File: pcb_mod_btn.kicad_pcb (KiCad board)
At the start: 2 copper layers, 116.1 x 100.1 mm, 50 parts, among them J1 leds_1, J10 leds_2, J11 led_3, J12 btn_3, J13 leds_4, J14 leds_4, J15 leds_4, J16 leds_4, J17 btn_4, J18 leds_5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

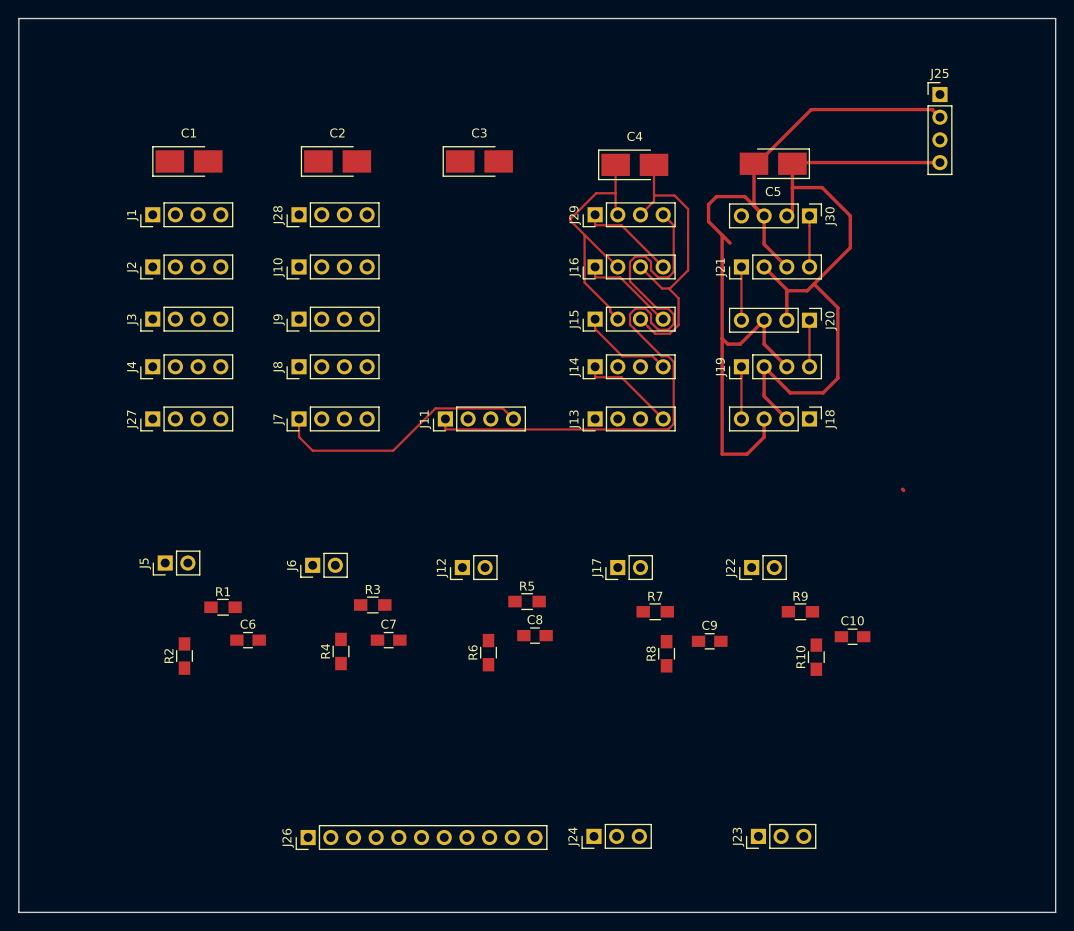
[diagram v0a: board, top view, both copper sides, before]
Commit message: footprints para tornillos, modulo botones terminado, todo marcas pin 1 headers
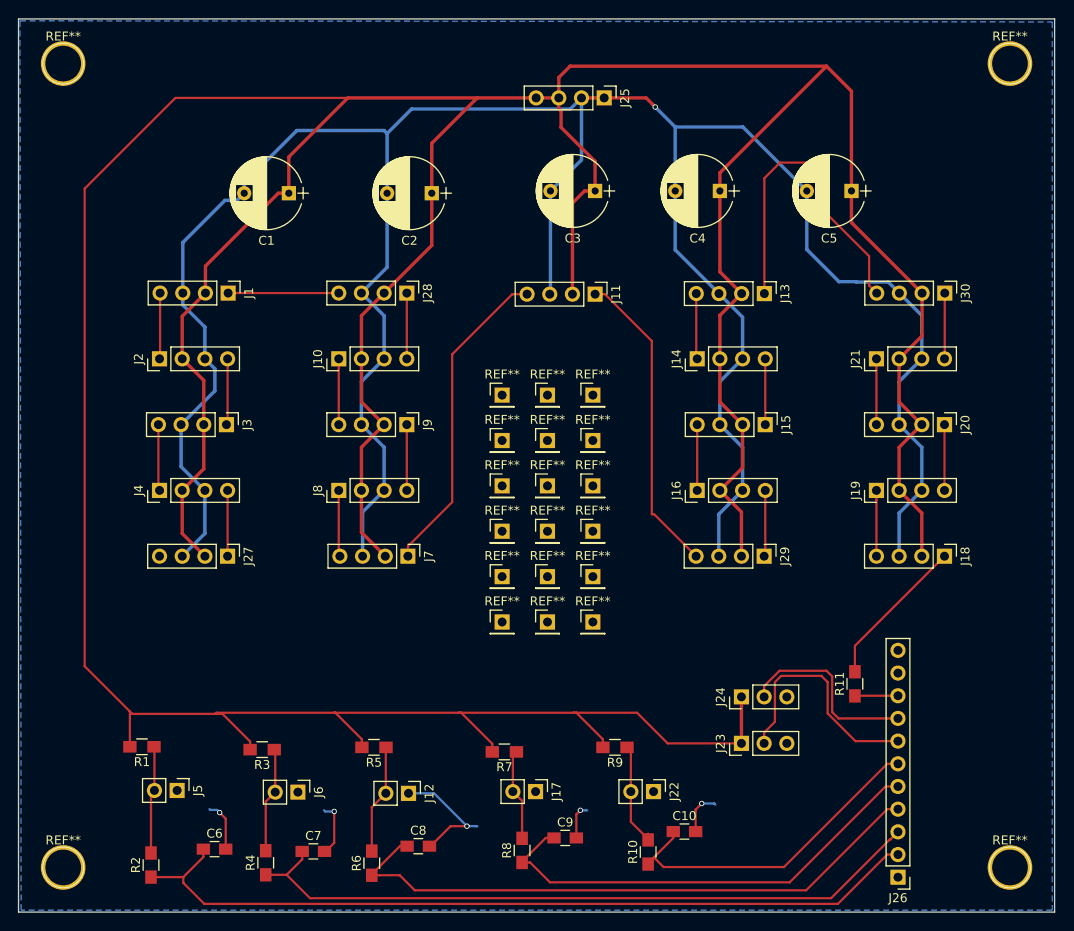
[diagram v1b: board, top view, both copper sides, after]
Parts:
- added R11: 240ohm, Resistors_SMD:R_0805_HandSoldering, F.Cu at (143.6, 103.4)
- added REF**: , Pin_Headers:Pin_Header_Straight_1x01_Pitch2.54mm, F.Cu at (114.3, 96.5)
- added REF**: , Pin_Headers:Pin_Header_Straight_1x01_Pitch2.54mm, F.Cu at (109.2, 86.4)
- added REF**: , Pin_Headers:Pin_Header_Straight_1x01_Pitch2.54mm, F.Cu at (104.1, 86.4)
- added REF**: , Pin_Headers:Pin_Header_Straight_1x01_Pitch2.54mm, F.Cu at (114.3, 86.4)
- added REF**: , Pin_Headers:Pin_Header_Straight_1x01_Pitch2.54mm, F.Cu at (114.3, 76.2)
- added REF**: , Pin_Headers:Pin_Header_Straight_1x01_Pitch2.54mm, F.Cu at (104.1, 76.2)
- added REF**: , Pin_Headers:Pin_Header_Straight_1x01_Pitch2.54mm, F.Cu at (109.2, 76.2)
- added REF**: 1pin, footprints:1pin, F.Cu at (161.0, 34.0)
- added REF**: 1pin, footprints:1pin, F.Cu at (55.0, 34.0)
- added REF**: 1pin, footprints:1pin, F.Cu at (55.0, 124.0)
- added REF**: 1pin, footprints:1pin, F.Cu at (161.0, 124.0)
- added REF**: , Pin_Headers:Pin_Header_Straight_1x01_Pitch2.54mm, F.Cu at (104.1, 96.5)
- added REF**: , Pin_Headers:Pin_Header_Straight_1x01_Pitch2.54mm, F.Cu at (109.2, 71.1)
- added REF**: , Pin_Headers:Pin_Header_Straight_1x01_Pitch2.54mm, F.Cu at (104.1, 71.1)
- added REF**: , Pin_Headers:Pin_Header_Straight_1x01_Pitch2.54mm, F.Cu at (114.3, 71.1)
- added REF**: , Pin_Headers:Pin_Header_Straight_1x01_Pitch2.54mm, F.Cu at (109.2, 96.5)
- added REF**: , Pin_Headers:Pin_Header_Straight_1x01_Pitch2.54mm, F.Cu at (109.2, 91.4)
- added REF**: , Pin_Headers:Pin_Header_Straight_1x01_Pitch2.54mm, F.Cu at (104.1, 91.4)
- added REF**: , Pin_Headers:Pin_Header_Straight_1x01_Pitch2.54mm, F.Cu at (114.3, 91.4)
- added REF**: , Pin_Headers:Pin_Header_Straight_1x01_Pitch2.54mm, F.Cu at (114.3, 81.3)
- added REF**: , Pin_Headers:Pin_Header_Straight_1x01_Pitch2.54mm, F.Cu at (104.1, 81.3)
- added REF**: , Pin_Headers:Pin_Header_Straight_1x01_Pitch2.54mm, F.Cu at (109.2, 81.3)
- C1, C2, C3, C4, C5: footprint Capacitors_Tantalum_SMD:CP_Tantalum_Case-T_EIA-3528-12_Hand -> Capacitors_THT:CP_Radial_D8.0mm_P5.00mm
- moved J26 66.2 mm to (148.5, 125.1), turned to 180 degrees
- moved J29 42.7 mm to (133.5, 89.2), turned to 270 degrees
- moved J25 37.6 mm to (115.6, 37.8), turned to 270 degrees
- moved C10 28.8 mm to (124.6, 120.0)
- moved R10 28.8 mm to (120.5, 122.3)
- moved J16 27.5 mm to (126.0, 81.8)
- moved J22 27.4 mm to (121.1, 115.5), turned to 270 degrees
- moved R8 27.3 mm to (106.4, 122.1)
- moved C9 27.3 mm to (111.2, 120.7)
- moved C8 27.0 mm to (94.8, 121.6)
- moved R6 27.0 mm to (89.5, 123.5)
- moved J17 26.7 mm to (107.9, 115.5), turned to 270 degrees
- moved J12 26.0 mm to (93.7, 115.7), turned to 270 degrees
- moved R9 25.7 mm to (116.8, 110.6), turned to 180 degrees
- moved J5 25.5 mm to (67.8, 115.4), turned to 270 degrees
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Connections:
- J26 pad 9: /data_leds -> Net-(J26-Pad9)
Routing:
- net +5V: track 110.5 -> 529.3 mm
- net GND: track 128.5 -> 340.6 mm, vias 0 -> 6
- net /btn_1: track 0.00 -> 91.6 mm
- net /btn_2: track 0.00 -> 78.3 mm
- net /btn_3: track 0.00 -> 68.7 mm
- net /btn_4: track 0.00 -> 52.2 mm
- net /leds_4: track 72.2 -> 34.8 mm
- net /btn_5: track 0.00 -> 37.4 mm
- net /leds_5: track 0.00 -> 36.7 mm
- net /pot_1: track 0.00 -> 26.5 mm
- net /pot_2: track 0.00 -> 21.4 mm
- net /data_leds: track 0.00 -> 17.1 mm
- net /leds_2: track 0.00 -> 12.4 mm
- net Net-(J12-Pad2): track 0.00 -> 12.3 mm
- net Net-(J5-Pad2): track 0.00 -> 12.1 mm
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- added copper zone on B.Cu, net GND
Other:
- board size 116.1 x 100.1 mm -> 116 x 100 mm
